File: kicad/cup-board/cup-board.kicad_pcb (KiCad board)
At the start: 4 copper layers, 68 x 68 mm, 102 parts, among them J2 EARCUP_SPKR, J7 CUP_IN (A2B + panel audio, ma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, J8 CUP_OUT (A2B to next cup), Q1 AO3401A, Q2 MMBT3904, U1 ADAU1861, U2 LSM6DSV16BX, U3 MAXM86161, U4 AQW612S, U5 AQW612S, U6 AD2428WBCPZ (sub-node), U7 TPS62161DSG (1V8), U8 ADP7118AUJZ-3.3-R7 (3V3_MIC), U9 ADP7118AUJZ-3.3-R7 (VLED)

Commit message: [LIMA] cup PCB: B-side trio routed + locked; 11 unconnected, 0 errors (WIP)
Co-Authored-By: Claude Opus 5.5 <noreply@anthropic.com>
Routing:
- net /DMIC_DATA: track 33.7 -> 153.2 mm, vias 2 -> 5
- net /I2S0_SDATAI: track 71.6 -> 2.16 mm
- net /I2S0_FSYNC: track 68.1 -> 0.00 mm, vias 2 -> 0
- net /1V8: track 11.6 -> 67.9 mm, vias 27 -> 25
- net /SDA: track 116.6 -> 63.6 mm, vias 5 -> 3
- net /I2S0_BCLK: track 74.4 -> 108.3 mm, vias 4 -> 10
- net /DMIC_CLK: track 30.8 -> 4.36 mm
- net /VIN_CUP: track 136.7 -> 110.6 mm, vias 4 -> 6
- net /GND: track 30.8 -> 52.3 mm, vias 87 -> 74
- net /B_SWP: track 0.94 -> 19.0 mm, vias 1 -> 2
- net /A_AP: track 16.0 -> 5.02 mm, vias 2 -> 0
- net /3V3_MIC: track 75.1 -> 65.3 mm, vias 0 -> 2
- net /B_BN: track 0.00 -> 6.34 mm
- net /SCL: track 0.00 -> 6.28 mm, vias 0 -> 2
- net /B_LINE_N: track 28.9 -> 23.6 mm, vias 3 -> 5
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
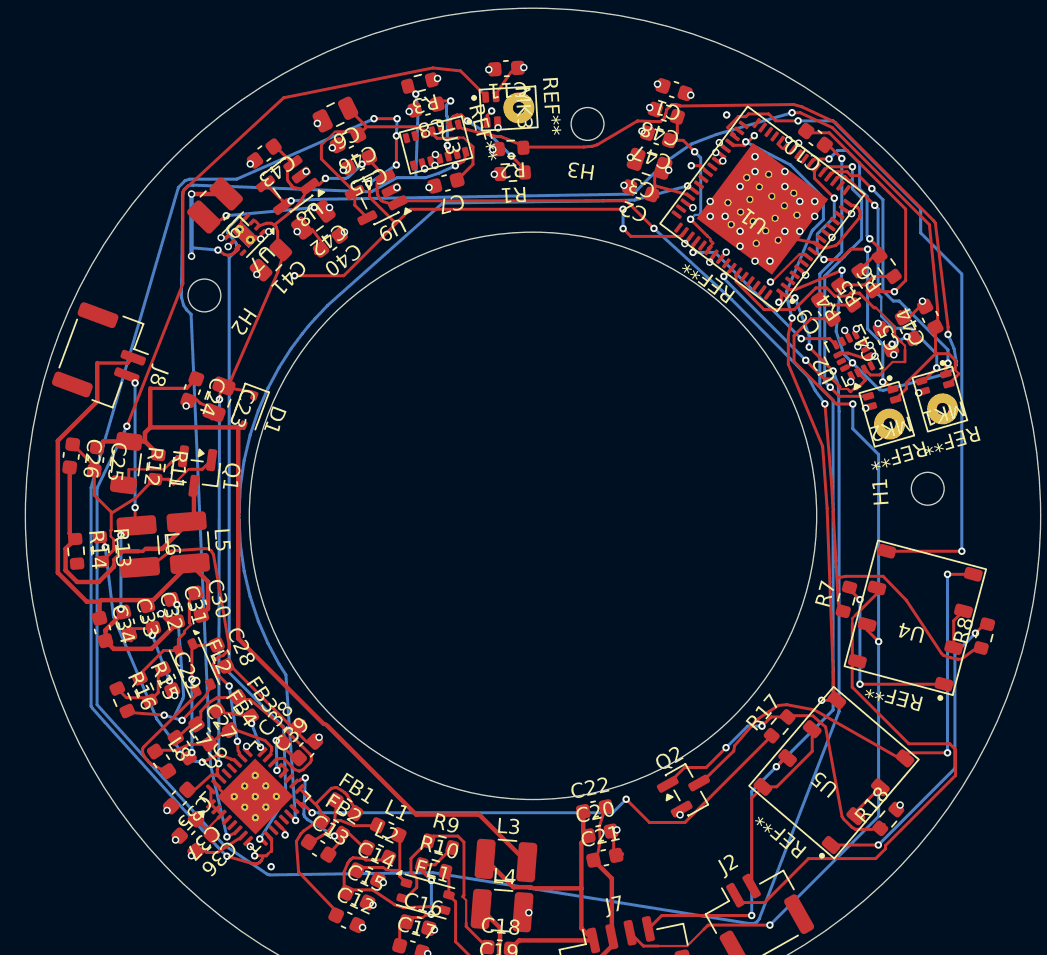
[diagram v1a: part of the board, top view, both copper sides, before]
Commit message: [LIMA] cup PCB: U6 bus nets re-routed with In2 available - 10 unconnected, 0 errors (WIP)
Co-Authored-By: Claude Opus 5.5 <noreply@anthropic.com>
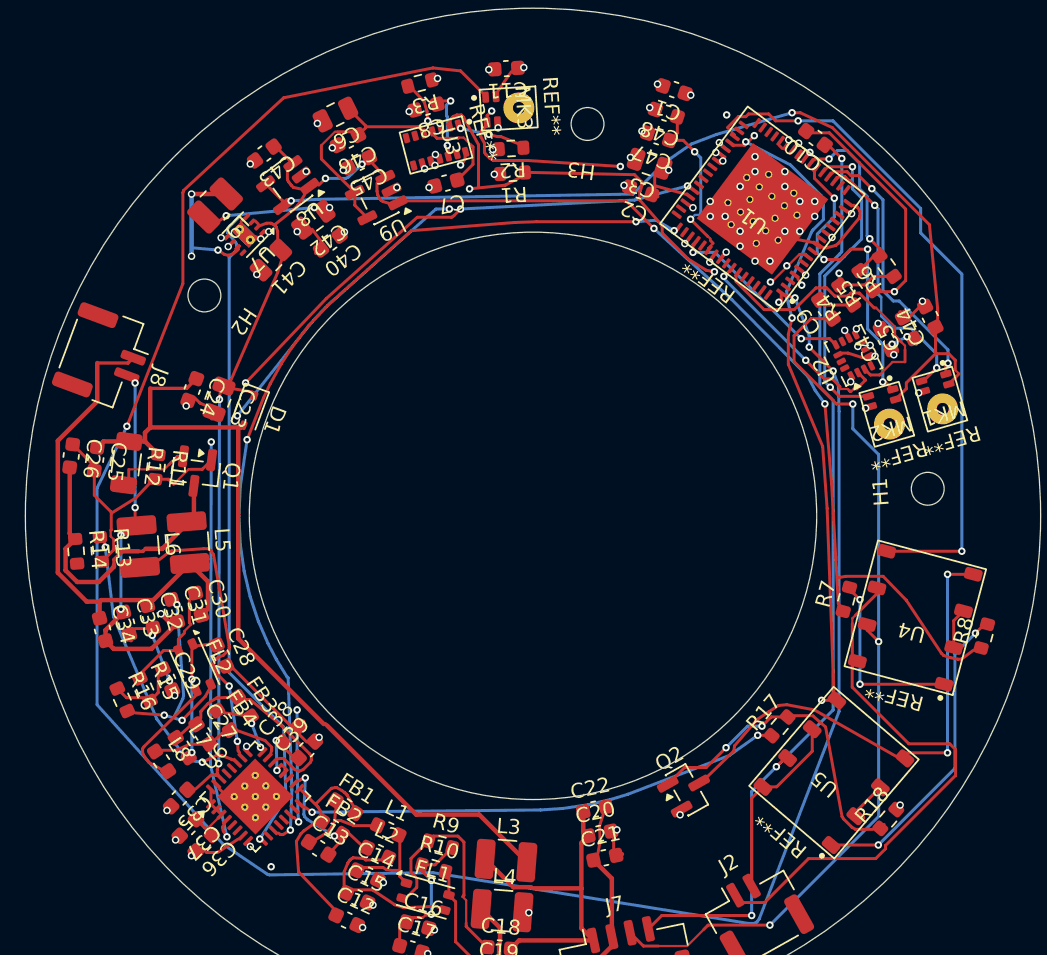
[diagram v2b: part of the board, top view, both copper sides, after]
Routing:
- net /I2S0_BCLK: track 108.3 -> 0.00 mm, vias 10 -> 0
- net /SCL: track 6.28 -> 84.3 mm, vias 2 -> 7
- net /I2S0_FSYNC: track 0.00 -> 63.7 mm, vias 0 -> 4
- net /PPG_INT: track 69.6 -> 6.92 mm, vias 3 -> 2
- net /SDA: track 63.6 -> 3.95 mm, vias 3 -> 2
- net /DMIC_CLK: track 4.36 -> 29.7 mm, vias 2 -> 4
- net /ADC2_P: track 3.90 -> 13.0 mm, vias 0 -> 2
- net /K2_CTL: track 35.3 -> 31.9 mm
- net /I2S0_SDATAI: track 2.16 -> 0.00 mm, vias 2 -> 0
- net /I2S0_SDATAO: track 64.0 -> 65.4 mm, vias 2 -> 5

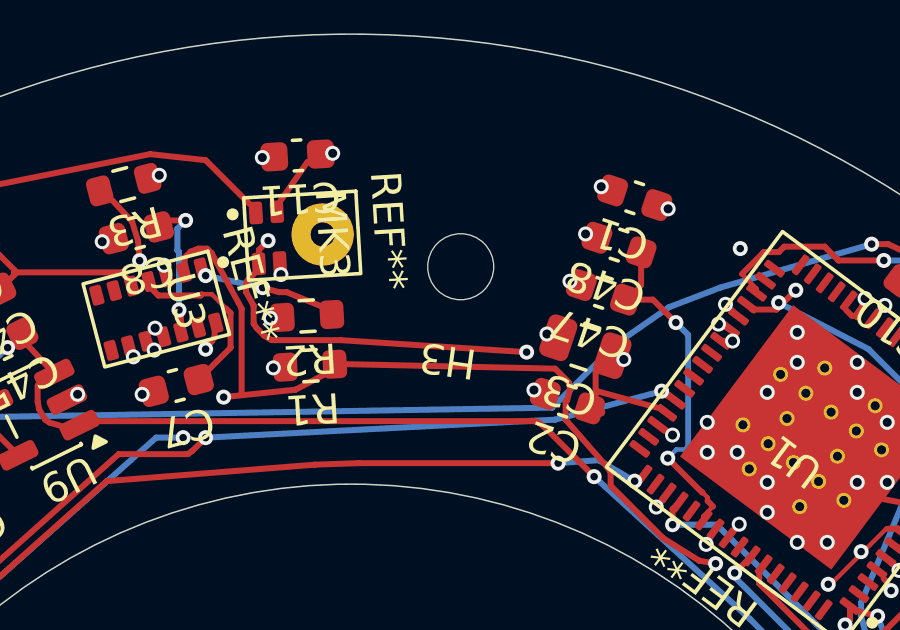
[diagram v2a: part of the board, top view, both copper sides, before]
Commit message: [LIMA] cup board: H3 removed (Peter - two M2 holes is fine); it blocked the top routing corridor
Schematic via Konnect delete_schematic_component; footprint via pcbnew (KiCad closed). Parity 0.

Co-Authored-By: Claude Opus 5.5 <noreply@anthropic.com>
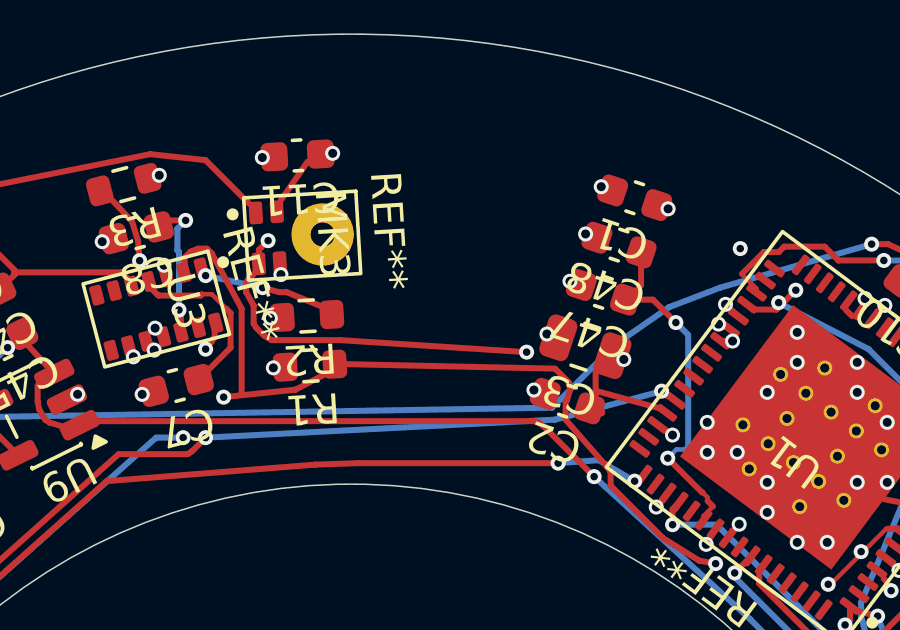
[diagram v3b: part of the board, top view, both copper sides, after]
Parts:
- removed H3: M2, MountingHole:MountingHole_2.2mm_M2
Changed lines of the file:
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@@
 		)
-	)
-	(footprint "MountingHole:MountingHole_2.2mm_M2"
-		(layer "F.Cu")
-		(at 153.653 73.753 172.08)
-		(property "Reference" "H3"
-			(at 0 -3.149999 172.08)
-			(unlocked yes)
-			(layer "F.SilkS")
-			(effects
-				(font
-					(size 1 1)
-					(line_spacing 0)
-				)
-			)
-		)
-		(property "Value" "M2"
-			(at 0 3.149999 172.08)
-			(unlocked yes)
-			(layer "F.SilkS")
-			(hide yes)
-			(effects
-				(font
-					(size 1 1)
-					(line_spacing 0)
-				)
-			)
-		)
-		(property "Datasheet" ""
-			(at 0 0 172.08)
-			(layer "F.Fab")
-			(hide yes)
-			(effects
-				(font
-					(size 1.27 1.27)
-				)
-			)
-		)
-		(property "Description" ""
-			(at 0 0 172.08)
-			(layer "F.Fab")
-			(hide yes)
-			(effects
-				(font
-					(size 1.27 1.27)
-				)
-			)
-		)
-		(duplicate_pad_numbers_are_jumpers no)
-		(fp_circle
-			(center 0 0)
-			(end 2.2 0)
-			(stroke
-				(width 0.15)
-				(type solid)
-			)
-			(fill no)
-			(layer "Cmts.User")
-		)
-		(fp_circle
-			(center 0 0)
-			(end 2.449999 0)
-			(stroke
-				(width 0.05)
-				(type solid)
-			)
-			(fill no)
-			(layer "F.CrtYd")
-		)
-		(fp_text user "${REFERENCE}"
-			(at 0 0 172.08)
-			(unlocked yes)
-			(layer "F.Fab")
-			(effects
-				(font
-					(size 1 1)
-					(thickness 0.15)
-				)
-			)
-		)
-		(pad "" np_thru_hole circle
-			(at 0 0 172.08)
-			(size 2.2 2.2)
-			(drill 2.2)
-			(layers "*.Cu" "*.Mask")
-		)
-		(embedded_fonts no)
 	)
 	(footprint "Capacitor_SMD:C_0603_1608Metric"

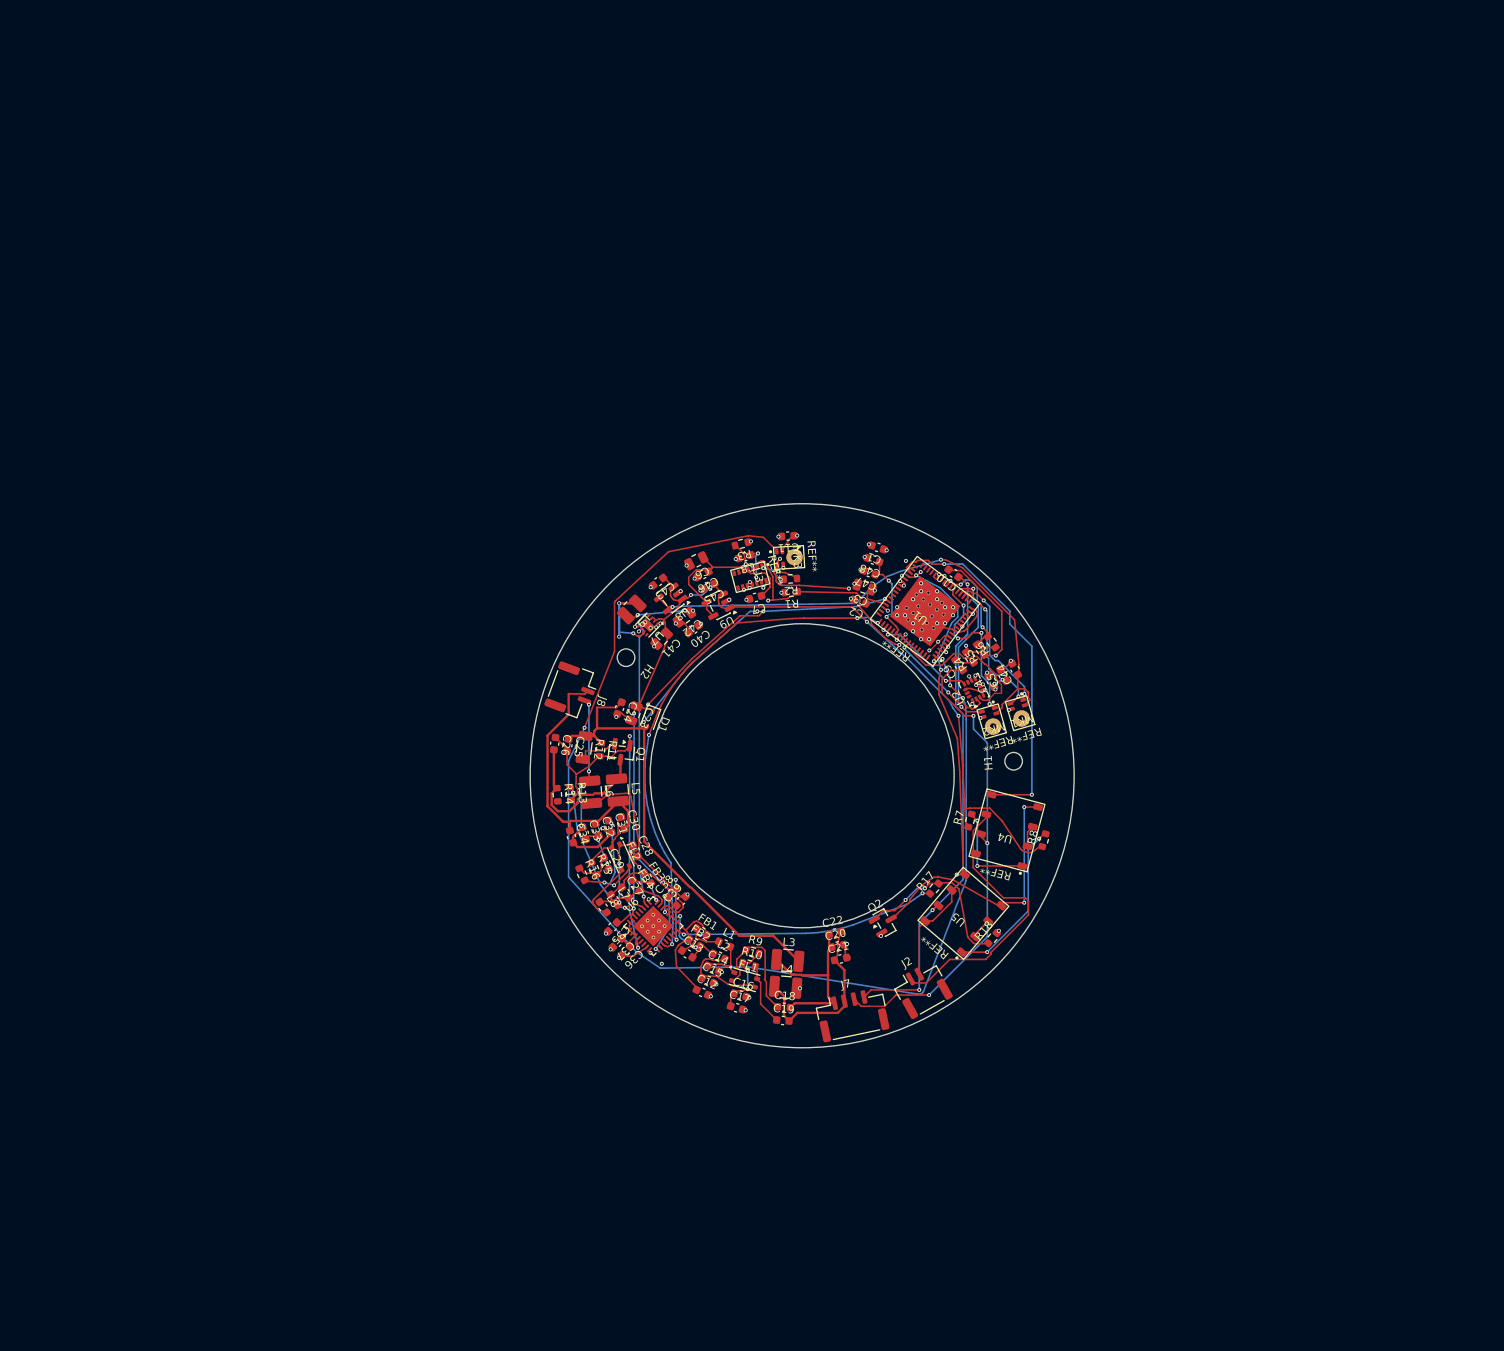
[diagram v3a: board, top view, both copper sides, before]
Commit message: [LIMA] cup PCB: ring 72/38 (Peter), mics on flex ZIFs J9-J11, re-placed; planes + fanout (pre-route)
syncnet.py (pcbnew netlist sync, keeps 3D models) adds J9-J11, drops MK1-3/H3; parity 0.
ring_placement.py: RO 36; connector radius from its own courtyard; back-to-back ZIF slot -
J10 (MK2, feedback mic) opens inward toward the driver, J9 (MK1, feed-forward) outward. 356 of 360 deg.
U6 turned +90 in place, decaps seated end-on. DRC 0 errors, 153 unconnected (to route).

Co-Authored-By: Claude Opus 5.5 <noreply@anthropic.com>
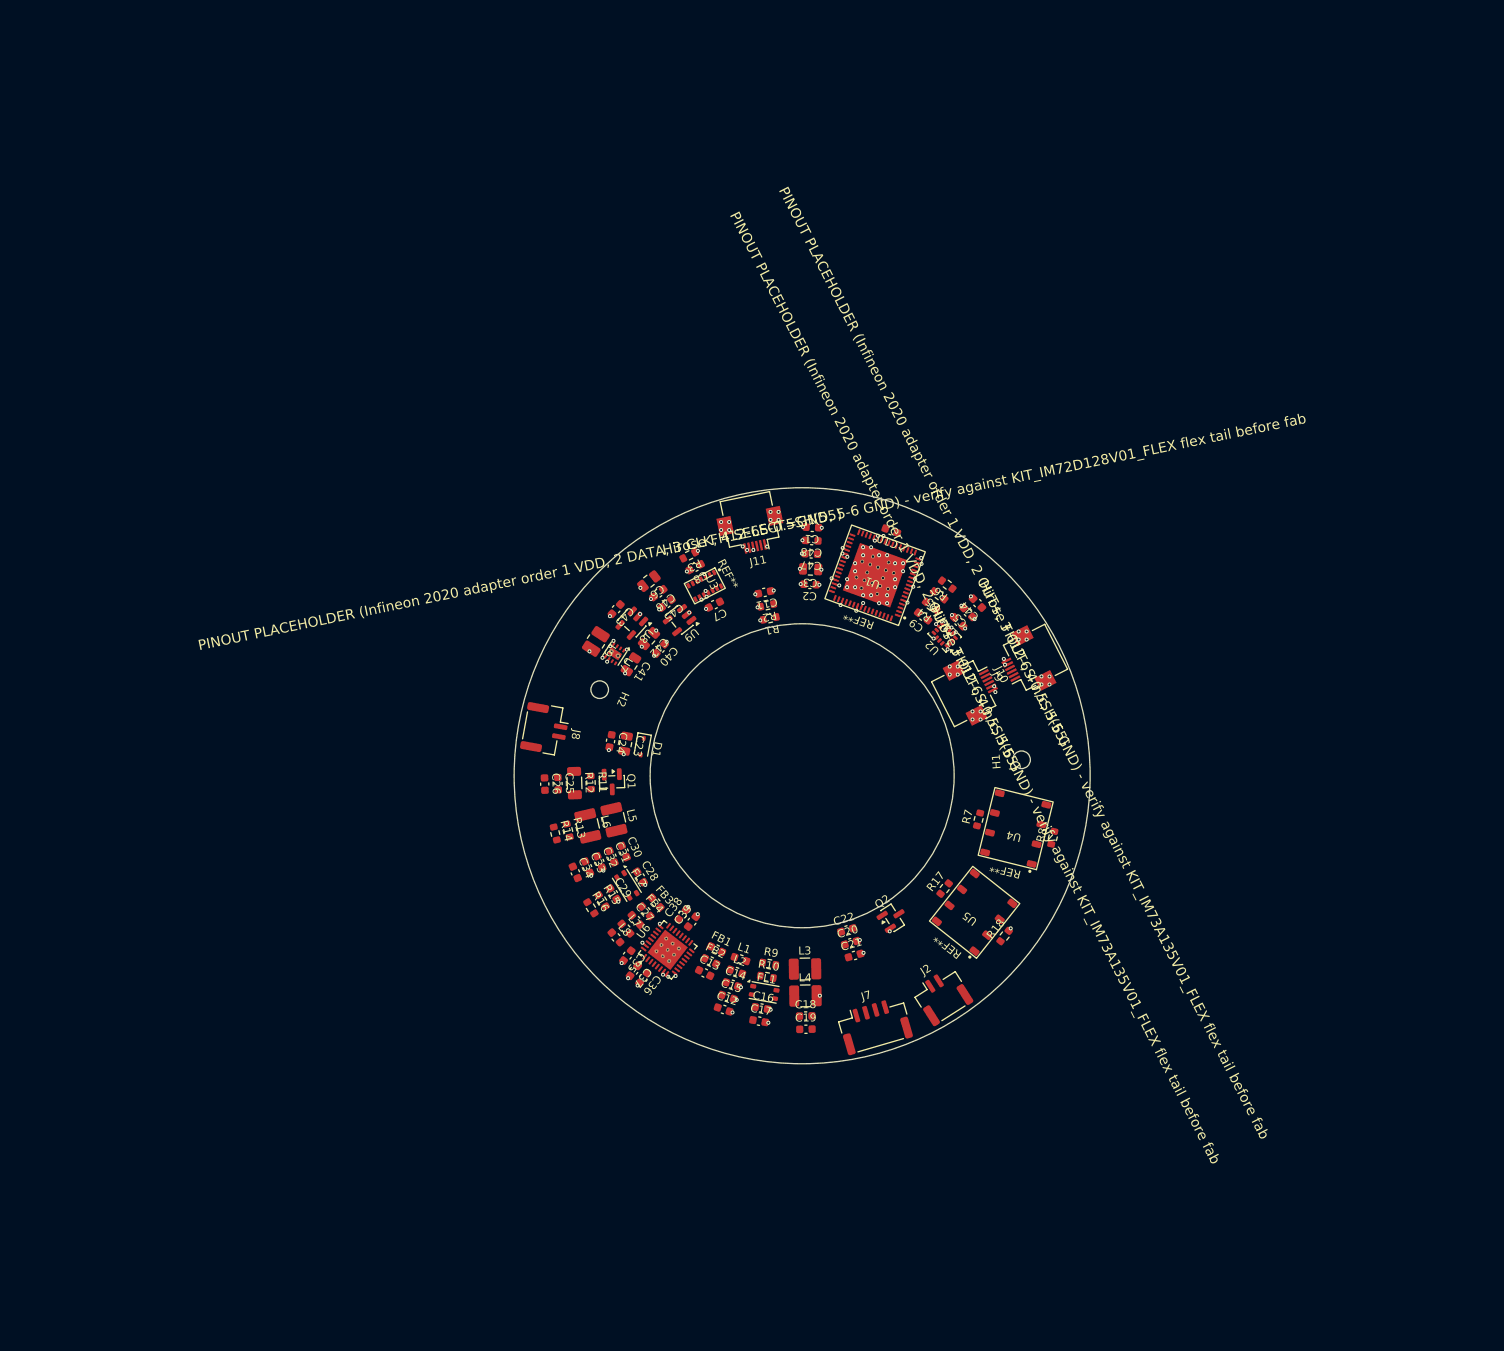
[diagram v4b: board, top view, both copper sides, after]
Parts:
- removed MK1, MK2: IM73A135V01, Infineon:Infineon_PG-LLGA-5_4x3mm_IM73A135_IM72D128
- removed MK3: IM72D128VV01, Infineon:Infineon_PG-LLGA-5_4x3mm_IM73A135_IM72D128
- added J10: MK2 flex (IM73A135), Connector_FFC-FPC:Hirose_FH12-6S-0.5SH_1x06-1MP_P0.50mm_Horizontal, F.Cu at (171.6, 89.0)
- added J11: MK3 flex (IM72D128 PDM), Connector_FFC-FPC:Hirose_FH12-6S-0.5SH_1x06-1MP_P0.50mm_Horizontal, F.Cu at (143.7, 69.5)
- added J9: MK1 flex (IM73A135 FF/FB), Connector_FFC-FPC:Hirose_FH12-6S-0.5SH_1x06-1MP_P0.50mm_Horizontal, F.Cu at (177.7, 85.9)
- moved C44 9.50 mm to (171.9, 78.4), turned to 134.56 degrees
- moved C10 9.42 mm to (161.1, 69.4), turned to 160.01 degrees
- moved R6 9.08 mm to (168.1, 76.1), turned to 142.79 degrees
- moved C5 8.98 mm to (170.7, 79.6), turned to 134.56 degrees
- moved R5 8.57 mm to (167.1, 77.4), turned to 142.79 degrees
- moved C1 8.55 mm to (151.3, 69.0), turned to 177.64 degrees
- moved C4 8.47 mm to (169.6, 80.7), turned to 134.56 degrees
- moved C48 8.09 mm to (151.2, 70.6), turned to 177.64 degrees
- moved R4 8.07 mm to (166.1, 78.8), turned to 142.79 degrees
- moved U2 7.71 mm to (167.8, 82.5), turned to 134.56 degrees
- moved U1 7.70 mm to (159.1, 74.9), turned to 160.01 degrees
- moved C47 7.63 mm to (151.1, 72.3), turned to 177.64 degrees
- moved C11 7.62 mm to (145.3, 77.1), turned to -168.4 degrees
- moved C9 7.56 mm to (165.1, 80.1), turned to 142.79 degrees
- moved C3 7.11 mm to (151.1, 74.2), turned to 177.64 degrees
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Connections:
- U1 pad 19: Net-(MK1-OUT-) -> /MK1_OUTN
- U1 pad 20: Net-(MK1-OUT+) -> /MK1_OUTP
- U1 pad 21: Net-(MK2-OUT-) -> /MK2_OUTN
- U1 pad 22: Net-(MK2-OUT+) -> /MK2_OUTP
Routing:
- net /DMIC_DATA: track 153.2 -> 0.00 mm, vias 5 -> 0
- net /VIN_CUP: track 110.6 -> 0.00 mm, vias 6 -> 0
- net /SCL: track 84.3 -> 0.00 mm, vias 7 -> 0
- net /I2S0_SDATAO: track 65.4 -> 0.00 mm, vias 5 -> 0
- net /3V3_MIC: track 65.3 -> 0.00 mm, vias 2 -> 0
- net /XF_SEC_B: track 63.7 -> 0.00 mm, vias 3 -> 0
- net /I2S0_FSYNC: track 63.7 -> 0.00 mm, vias 4 -> 0
- net /XF_SEC_A: track 60.3 -> 0.00 mm, vias 3 -> 0
- net /V_NODE: track 57.7 -> 0.00 mm
- net /1V8: track 67.9 -> 11.6 mm, vias 25 -> 27
- net /HPOUTN: track 45.9 -> 0.00 mm, vias 2 -> 0
- net /HPOUTP: track 43.7 -> 0.00 mm, vias 4 -> 0
- net /SPKR_1: track 36.6 -> 0.00 mm
- net /B_LINE_P: track 34.1 -> 0.00 mm
- net /K2_SW: track 32.6 -> 0.00 mm, vias 2 -> 0
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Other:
- board size 68 x 68 mm -> 72 x 72 mm
